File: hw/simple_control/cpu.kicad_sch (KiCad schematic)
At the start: 11 parts, among them J601 Conn_01x04, J602 Raspberry_Pi_0_2_3, J603 Conn_01x03, SW602 SW_Push, U601 PicoW

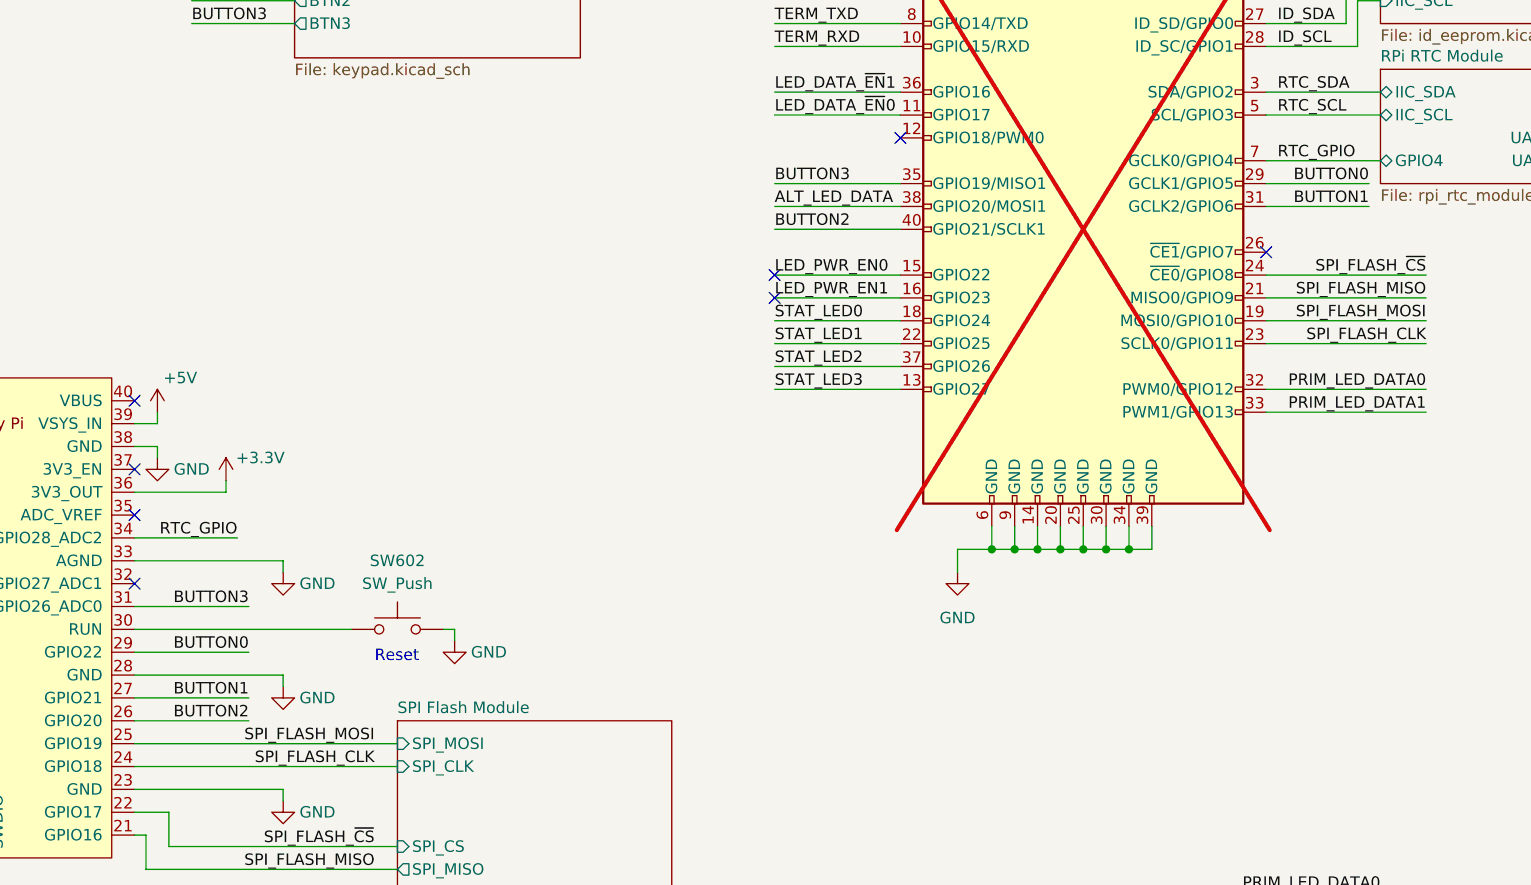
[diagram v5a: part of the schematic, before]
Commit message: chore(hw): keypad layout
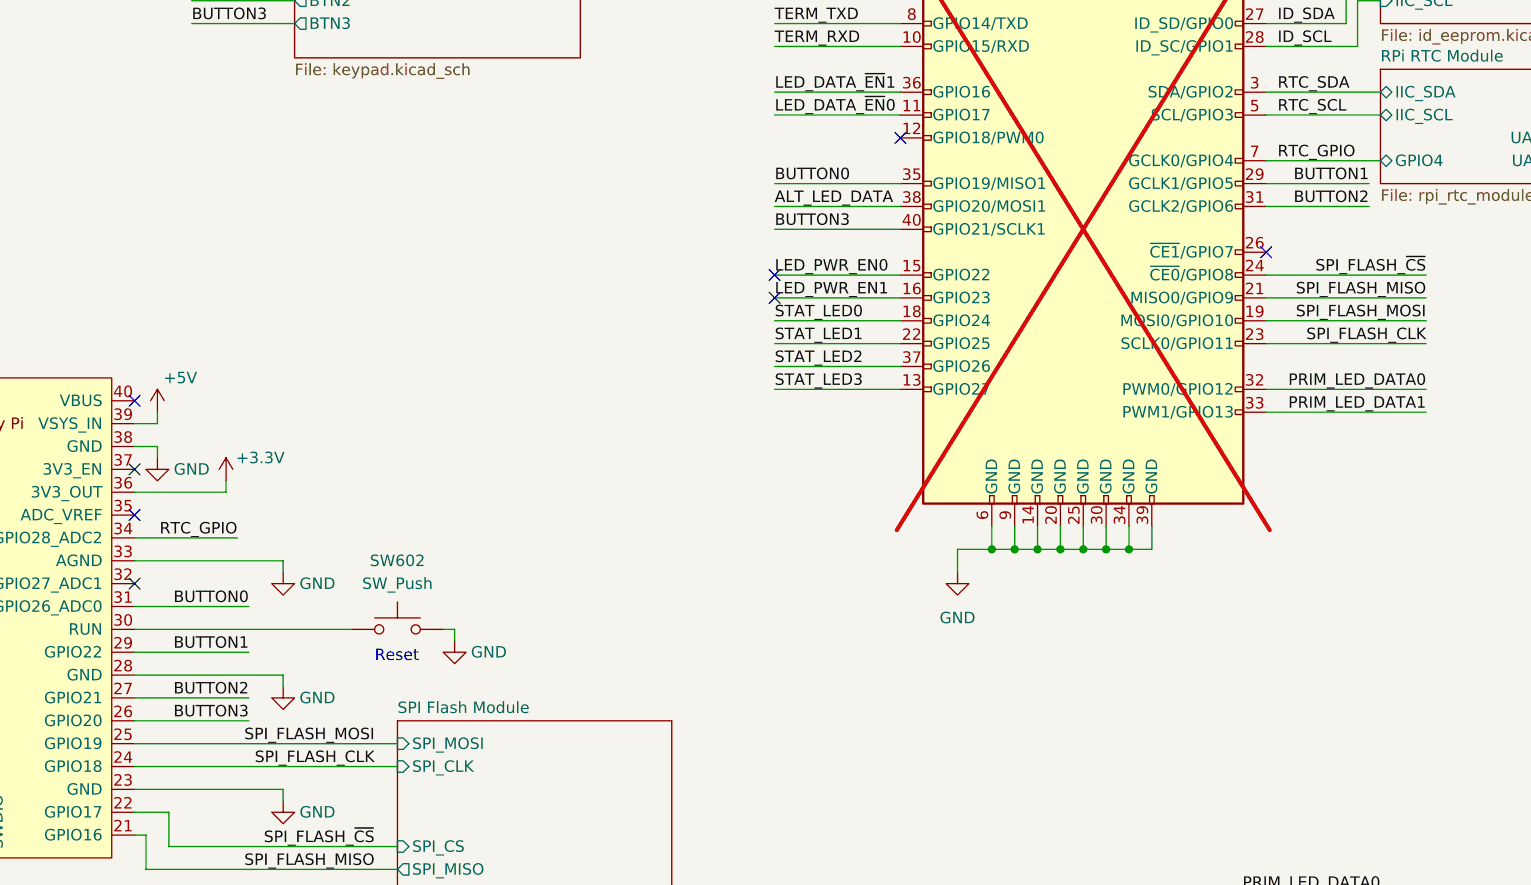
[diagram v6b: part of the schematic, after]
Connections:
- net BUTTON0: now also J602.35 (GPIO19/MISO1), U601.31 (GPIO26_ADC0); no longer J602.29 (GCLK1/GPIO5), U601.29 (GPIO22)
- net BUTTON1: now also J602.29 (GCLK1/GPIO5), U601.29 (GPIO22); no longer J602.31 (GCLK2/GPIO6), U601.27 (GPIO21)
- net BUTTON2: now also J602.31 (GCLK2/GPIO6), U601.27 (GPIO21); no longer J602.40 (GPIO21/SCLK1), U601.26 (GPIO20)
- net BUTTON3: now also J602.40 (GPIO21/SCLK1), U601.26 (GPIO20); no longer J602.35 (GPIO19/MISO1), U601.31 (GPIO26_ADC0)

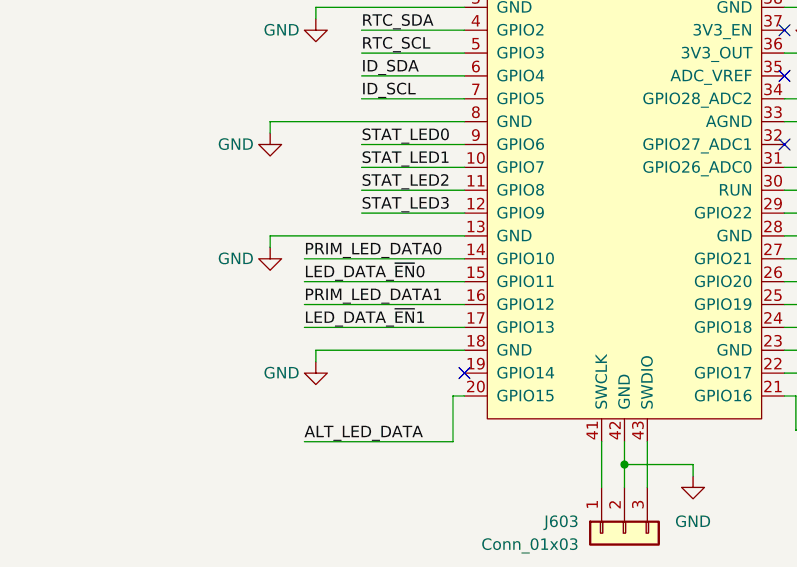
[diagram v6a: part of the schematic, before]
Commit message: chore(hw): move LED data outside of antenna keep-out area
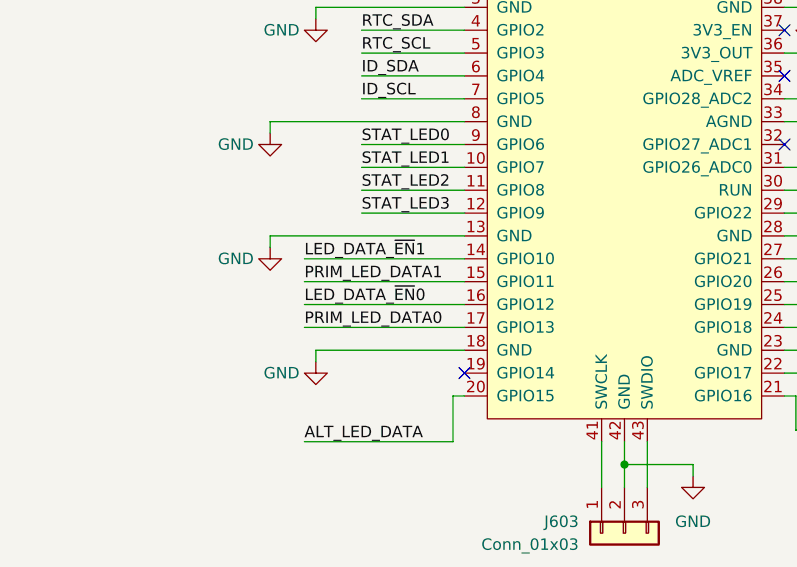
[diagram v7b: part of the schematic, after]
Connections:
- net LED_DATA_~{EN}0: now also U601.16 (GPIO12); no longer U601.15 (GPIO11)
- net LED_DATA_~{EN}1: now also U601.14 (GPIO10); no longer U601.17 (GPIO13)
- net PRIM_LED_DATA0: now also U601.17 (GPIO13); no longer U601.14 (GPIO10)
- net PRIM_LED_DATA1: now also U601.15 (GPIO11); no longer U601.16 (GPIO12)

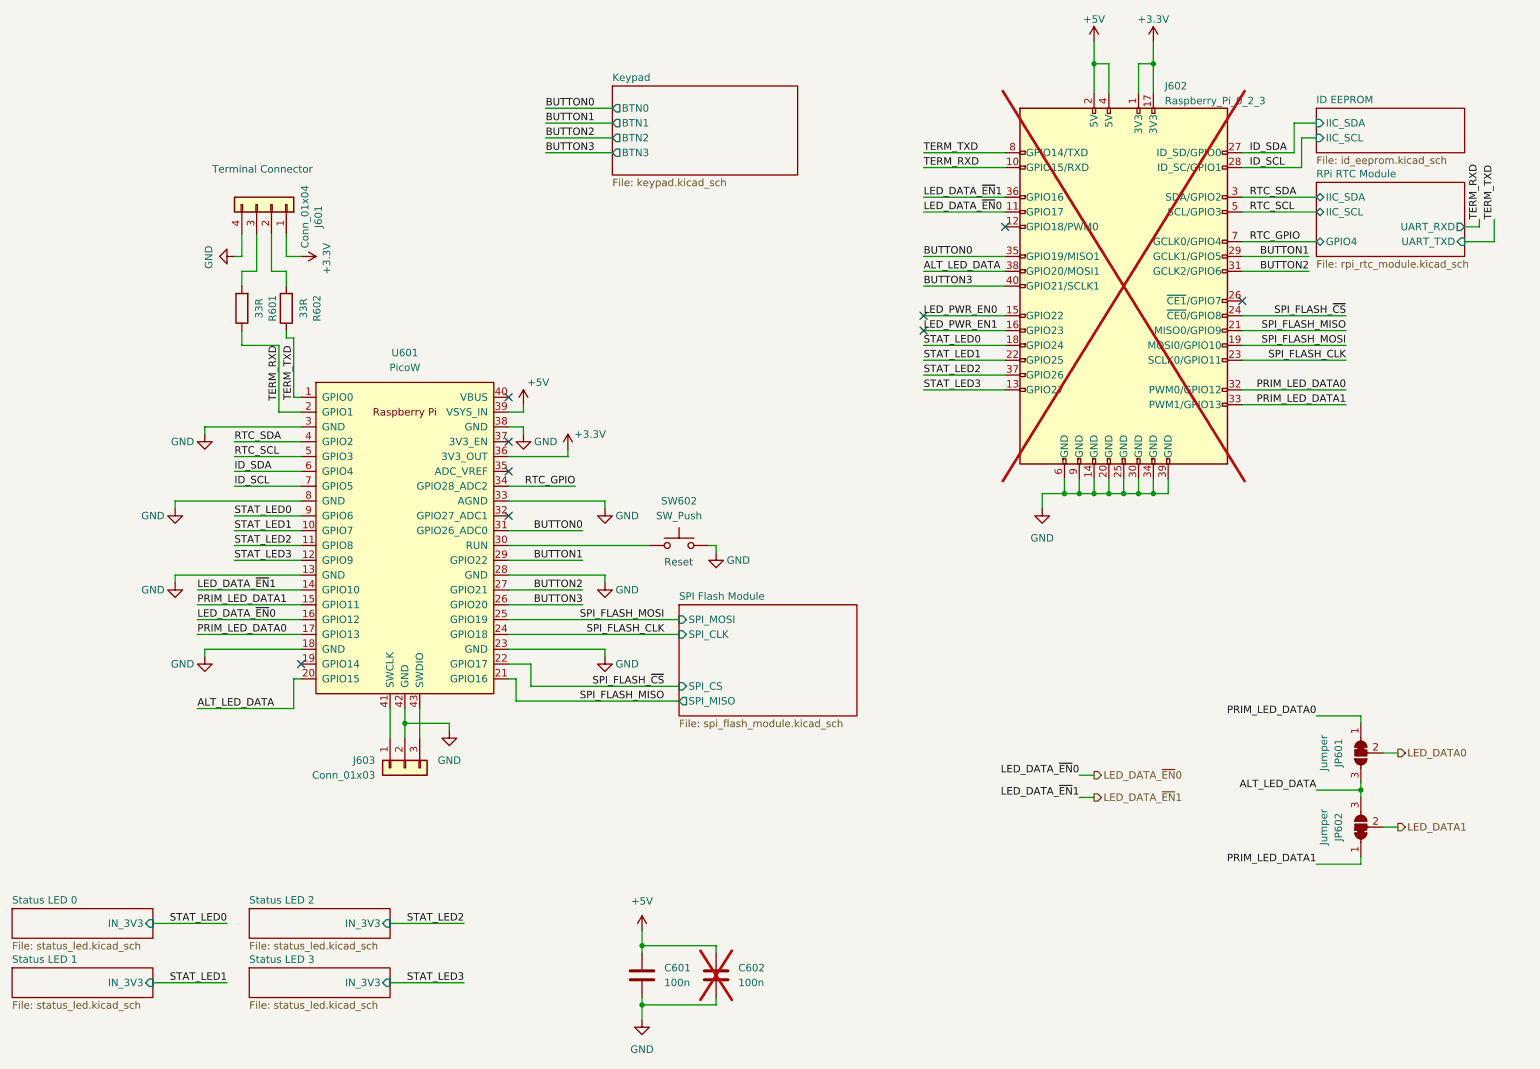
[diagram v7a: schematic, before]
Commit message: chore(hw): add VBUS back-feeding protection
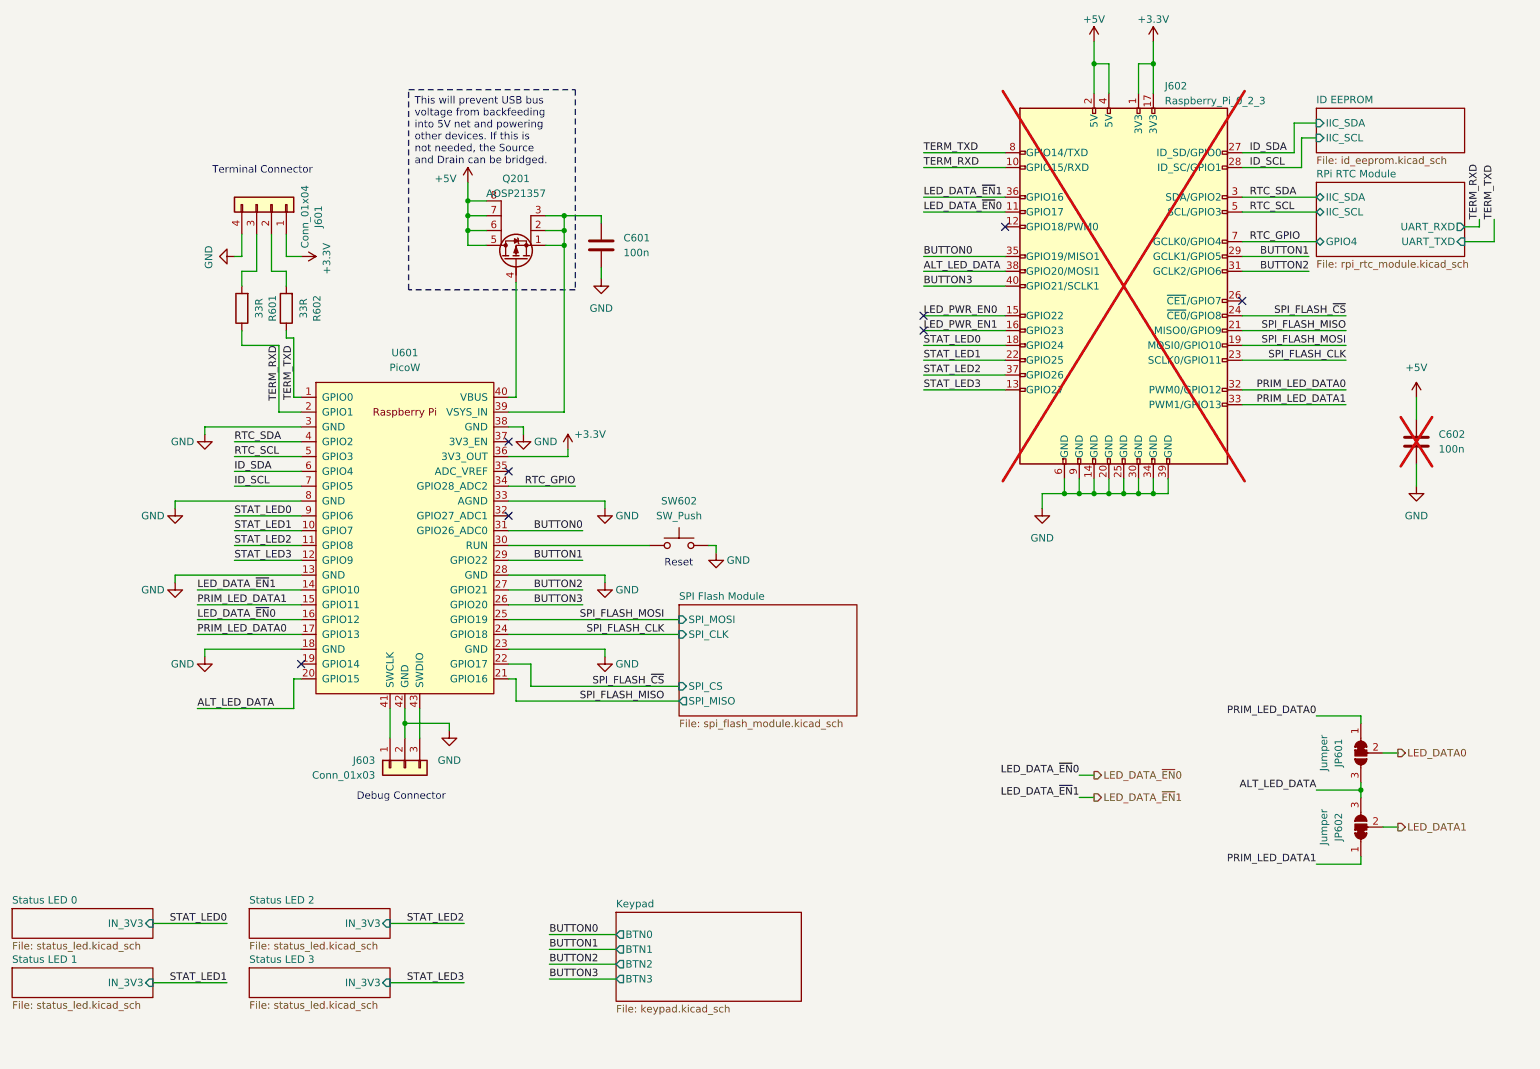
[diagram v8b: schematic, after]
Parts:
- added Q201: AOSP21357, Package_SO:SOIC-8_3.9x4.9mm_P1.27mm, symbol my:Q_PMOS_SSSGDDDD
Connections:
- net +5V: now also Q201.5 (D), Q201.6 (D), Q201.7 (D), Q201.8 (D); no longer C601.1, U601.39 (VSYS)
- net at U601.40 (VBUS): now also Q201.4 (G)
- new net: C601.1, Q201.1 (S), Q201.2 (S), Q201.3 (S), U601.39 (VSYS)
- no-connect marks 9 -> 8
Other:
- note added: "Debug Connector"
- moved on the sheet: C601, C602
